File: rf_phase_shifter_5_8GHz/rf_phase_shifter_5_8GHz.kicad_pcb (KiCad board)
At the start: 2 copper layers, 30.6 x 21 mm, 16 parts, among them J1 CON-SMA-EDGE-S, J2 CON-SMA-EDGE-S, J3 CON-SMA-EDGE-S

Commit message: update
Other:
- board text added: "Analog RF phase shifter 5.8 GHz Marcin Wachowiak, Poland"
- board text removed: "Analog RF phase shifter 5.8GHz Marcin Wachowiak, Poland"

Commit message: added info about substrate thickness
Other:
- board text added: "Substrate: FR4, thickness: 0.6 mm"

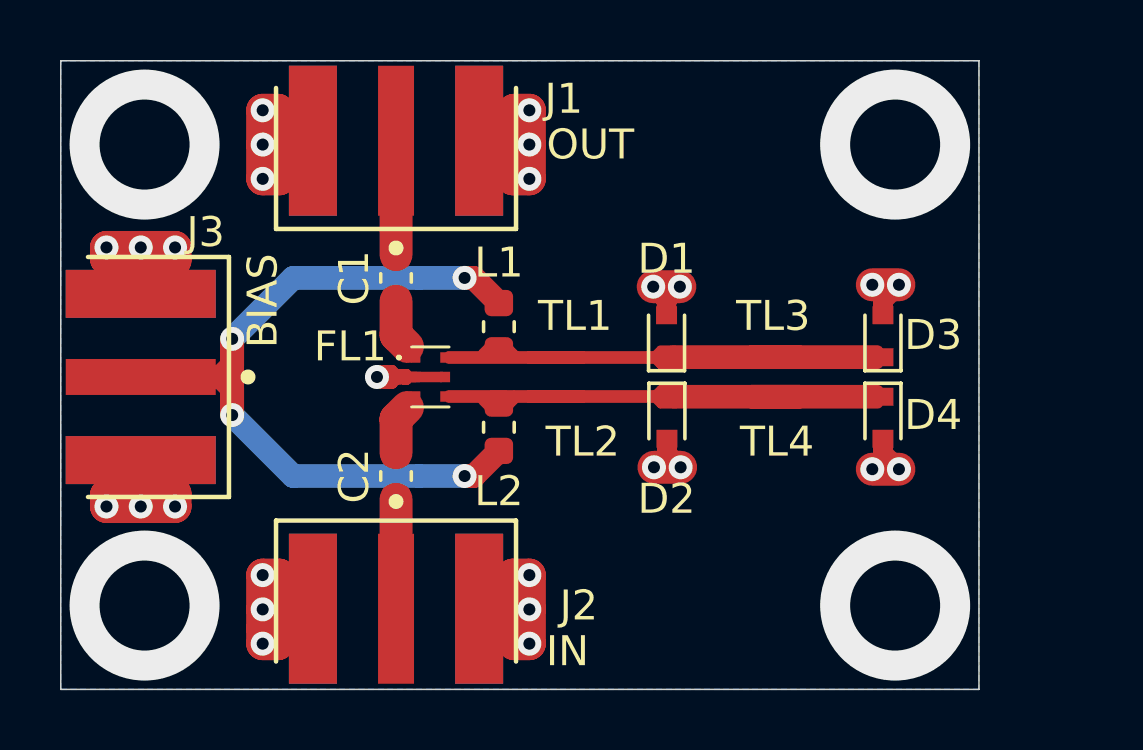
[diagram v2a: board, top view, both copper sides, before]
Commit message: Finished layout of second prototypes
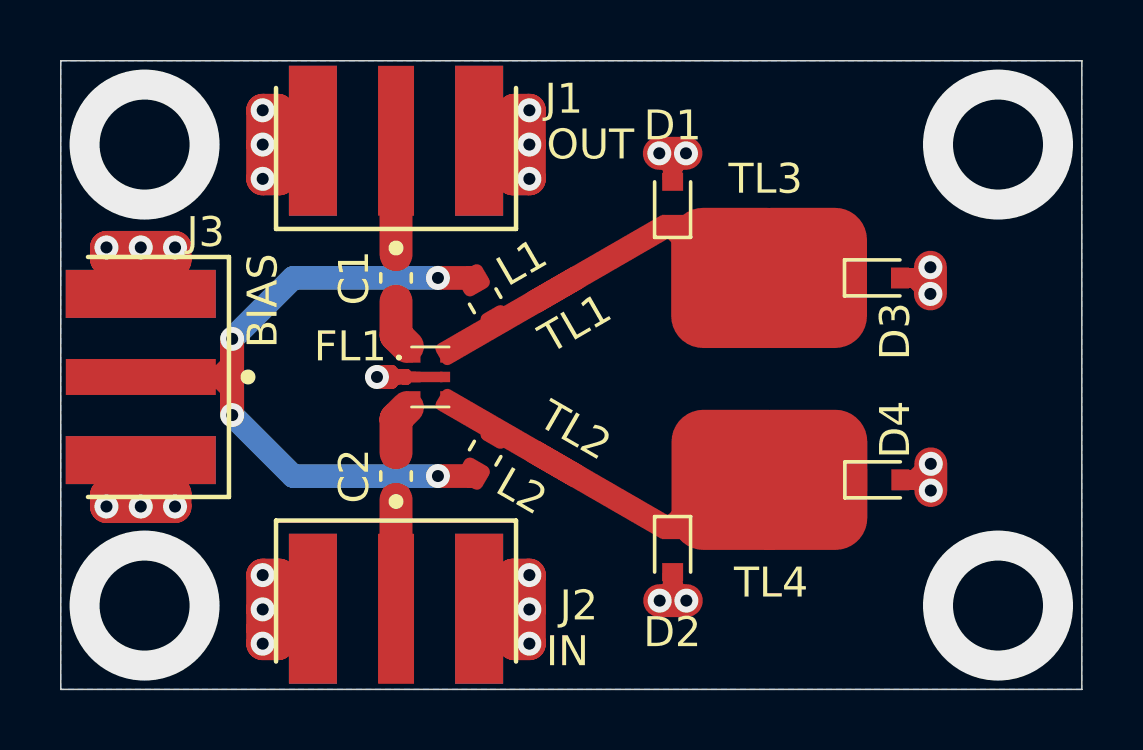
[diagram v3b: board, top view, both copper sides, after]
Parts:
- D1, D2, D3, D4: value BBY66_02V -> SMV1763-079LF
- moved D1 4.45 mm to (93.7, 53.1)
- moved D2 4.45 mm to (93.7, 64.7)
- moved TL4 2.78 mm to (96.9, 62.4)
- moved TL3 2.65 mm to (96.9, 55.6)
- moved TL1 2.25 mm to (89.8, 56.0), turned to 30 degrees
- moved TL2 2.25 mm to (89.8, 61.8), turned to 330 degrees
- moved D4 2.07 mm to (100.6, 62.4), turned to 0 degrees
- moved D3 1.95 mm to (100.6, 55.6), turned to 0 degrees
- moved L1 0.98 mm to (87.4, 56.4), turned to 300 degrees
- moved L2 0.98 mm to (87.4, 61.5), turned to 60 degrees
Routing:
- net Net-(D2-Pad1): track 9.90 -> 0.48 mm
- net Net-(D1-Pad1): track 6.29 -> 0.48 mm
- net Net-(J3-Pad1): track 28.3 -> 26.0 mm
- net Net-(FL1-Pad4): track 1.17 -> 0.00 mm
- net Net-(FL1-Pad6): track 0.90 -> 0.00 mm
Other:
- board size 30.6 x 21 mm -> 34 x 21 mm
